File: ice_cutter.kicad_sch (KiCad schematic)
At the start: 92 parts, among them J1 Conn_01x01_Male, J2 Barrel_Jack, J3 Conn_01x03_Male, J4 Conn_01x01_Male, J5 Conn_02x03_Odd_Even, M1 Motor_Servo, M2 Motor_Servo, Q1 Q_PMOS_GSD, Q10 Q_NPN_EBC, Q11 Q_NMOS_GSD, Q2 Q_PMOS_GSD, Q3 Q_PMOS_GSD, Q4 Q_PNP_EBC, Q5 Q_NMOS_GSD, Q6 Q_PNP_EBC, Q7 Q_NMOS_GSD, Q8 Q_NPN_EBC, Q9 Q_NPN_EBC, SW1 SW_Push, SW2 SW_Push, SW3 SW_Push, U1 LM317_TO-252, U10 TMP117, U11 TM1620, U2 LM317_TO-252, U3 INA219AxD, U4 LM317_TO-252, U5 INA219AxD, U6 FJ4301AH, U7 FJ4301AH, U8 STM32G030XX, U9 SHT30-DIS

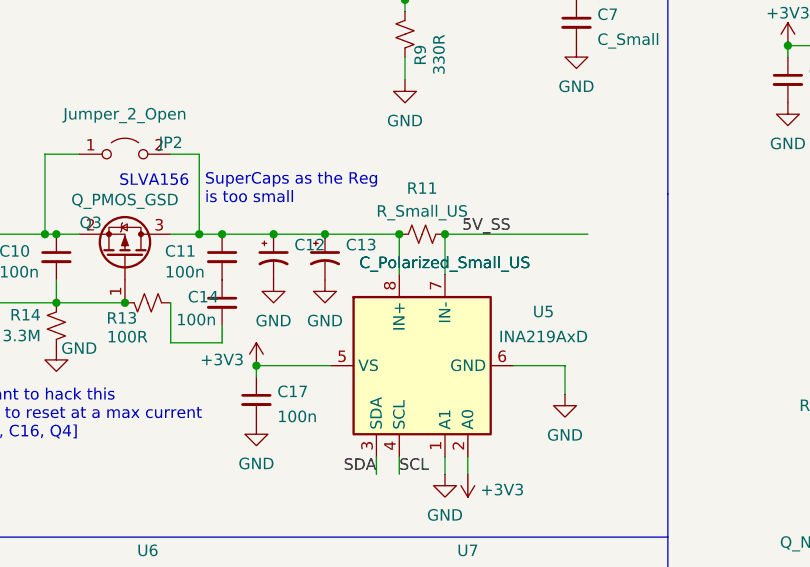
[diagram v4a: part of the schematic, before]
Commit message: added barrel jack and super caps
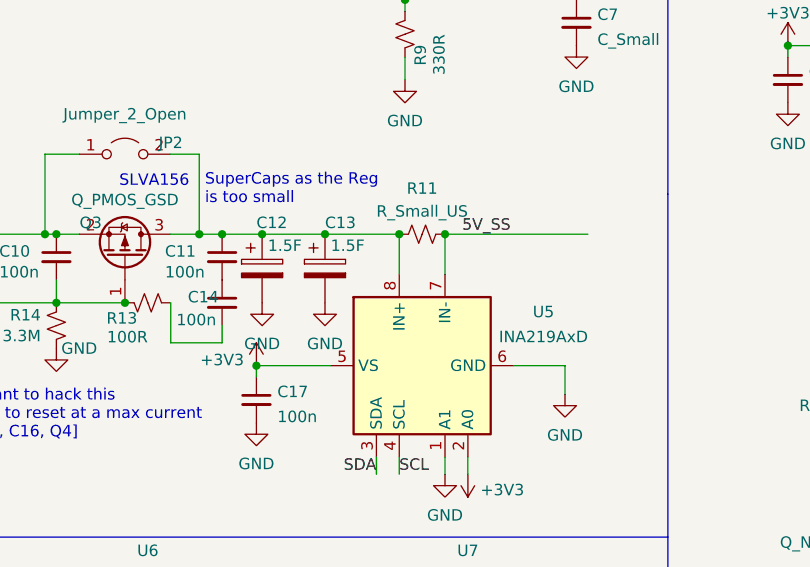
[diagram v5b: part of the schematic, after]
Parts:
- removed C12, C13: C_Polarized_Small_US, symbol Device:C_Polarized_Small_US
- added C12, C13: 1.5F, MyLibs:SP-5R5-Z155VY, symbol Device:C_Polarized
- J2: footprint (none) -> UCT:Barrel_Jack_2A_C84007
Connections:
- net GND: now also C12.2, C13.2
- net at C11.1, JP2.2 (B), Q3.3 (D)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: now also C12.1, C13.1
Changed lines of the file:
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@@
   (junction (at 238.76 148.59) (diameter 0) (color 0 0 0 0)
   )
+  (junction (at 161.29 60.325) (diameter 0) (color 0 0 0 0)
+  )
   (junction (at 181.61 60.325) (diameter 0) (color 0 0 0 0)
   )
   (junction (at 247.65 143.51) (diameter 0) (color 0 0 0 0)
   )
-  (junction (at 162.56 60.325) (diameter 0) (color 0 0 0 0)
-  )
   (junction (at 261.62 143.51) (diameter 0) (color 0 0 0 0)
   )
@@
   (junction (at 125.73 60.325) (diameter 0) (color 0 0 0 0)
   )
+  (junction (at 168.275 60.325) (diameter 0) (color 0 0 0 0)
+  )
   (junction (at 248.92 92.71) (diameter 0) (color 0 0 0 0)
   )
@@
   (junction (at 120.65 60.325) (diameter 0) (color 0 0 0 0)
   )
-  (junction (at 168.275 60.325) (diameter 0) (color 0 0 0 0)
-  )
   (junction (at 138.43 60.325) (diameter 0) (color 0 0 0 0)
   )
@@
     (stroke (width 0) (type default) (color 0 0 0 0))
   )
-  (wire (pts (xy 156.845 60.325) (xy 162.56 60.325))
-    (stroke (width 0) (type default) (color 0 0 0 0))
-  )
   (wire (pts (xy 27.305 75.565) (xy 33.655 75.565))
     (stroke (width 0) (type default) (color 0 0 0 0))
@@
     (stroke (width 0) (type default) (color 0 0 0 0))
   )
-  (wire (pts (xy 168.275 60.325) (xy 176.53 60.325))
+  (wire (pts (xy 156.845 60.325) (xy 161.29 60.325))
     (stroke (width 0) (type default) (color 0 0 0 0))
   )
@@
     (stroke (width 0) (type default) (color 0 0 0 0))
   )
+  (wire (pts (xy 168.275 60.325) (xy 176.53 60.325))
+    (stroke (width 0) (type default) (color 0 0 0 0))
+  )
   (wire (pts (xy 46.355 34.925) (xy 38.735 34.925))
     (stroke (width 0) (type default) (color 0 0 0 0))
@@
     (stroke (width 0) (type default) (color 0 0 0 0))
   )
-  (wire (pts (xy 162.56 60.325) (xy 168.275 60.325))
-    (stroke (width 0) (type default) (color 0 0 0 0))
-  )
   (polyline (pts (xy 87.63 55.88) (xy 87.63 87.63))
     (stroke (width 0) (type default) (color 0 0 0 0))
@@
     (stroke (width 0) (type default) (color 0 0 0 0))
   )
+  (wire (pts (xy 161.29 60.325) (xy 168.275 60.325))
+    (stroke (width 0) (type default) (color 0 0 0 0))
+  )
   (wire (pts (xy 81.915 169.545) (xy 81.915 172.72))
     (stroke (width 0) (type default) (color 0 0 0 0))
@@
     (pin "1")
   )
+  (symbol (lib_id "Device:C_Polarized") (at 168.275 64.135 0) (unit 1)
+    (in_bom yes) (on_board yes)
+    (property "Reference" "C13" (id 0) (at 168.275 59.055 0)
+      (effects (font (size 1.27 1.27)) (justify left))
+    )
+    (property "Value" "1.5F" (id 1) (at 168.91 61.595 0)
+      (effects (font (size 1.27 1.27)) (justify left))
+    )
+    (property "Footprint" "MyLibs:SP-5R5-Z155VY" (id 2) (at 169.2402 67.945 0)
+      (effects (font (size 1.27 1.27)) hide)
+    )
+    (property "Datasheet" "~" (id 3) (at 168.275 64.135 0)
+      (effects (font (size 1.27 1.27)) hide)
+    )
+    (property "LCSC" "C128277" (id 4) (at 168.275 64.135 0)
+      (effects (font (size 1.27 1.27)) hide)
+    )
+    (property "Populate" "Yes" (id 5) (at 168.275 64.135 0)
+      (effects (font (size 1.27 1.27)) hide)
+    )
+    (property "Price" "1.35" (id 6) (at 168.275 64.135 0)
+      (effects (font (size 1.27 1.27)) hide)
+    )
+    (pin "1")
+    (pin "2")
+  )
   (symbol (lib_id "Device:C_Small") (at 219.71 43.18 0) (unit 1)
     (in_bom yes) (on_board yes) (fields_autoplaced)
@@
     (pin "8")
   )
-  (symbol (lib_id "Device:C_Polarized_Small_US") (at 168.275 62.865 0) (unit 1)
-    (in_bom yes) (on_board yes)
-    (property "Reference" "C13" (id 0) (at 170.5864 61.5247 0)
-      (effects (font (size 1.27 1.27)) (justify left))
-    )
-    (property "Value" "C_Polarized_Small_US" (id 1) (at 172.085 63.5 0)
-      (effects (font (size 1.27 1.27)) (justify left))
-    )
-    (property "Footprint" "" (id 2) (at 168.275 62.865 0)
-      (effects (font (size 1.27 1.27)) hide)
-    )
-    (property "Datasheet" "~" (id 3) (at 168.275 62.865 0)
-      (effects (font (size 1.27 1.27)) hide)
-    )
-    (property "Populate" "Yes" (id 4) (at 168.275 62.865 0)
-      (effects (font (size 1.27 1.27)) hide)
-    )
-    (pin "1")
-    (pin "2")
-  )
   (symbol (lib_id "power:+5V") (at 91.44 71.755 0) (unit 1)
     (in_bom yes) (on_board yes)
@@
     (pin "2")
   )
+  (symbol (lib_id "Device:C_Polarized") (at 161.29 64.135 0) (unit 1)
+    (in_bom yes) (on_board yes)
+    (property "Reference" "C12" (id 0) (at 160.655 59.055 0)
+      (effects (font (size 1.27 1.27)) (justify left))
+    )
+    (property "Value" "1.5F" (id 1) (at 161.925 61.595 0)
+      (effects (font (size 1.27 1.27)) (justify left))
+    )
+    (property "Footprint" "MyLibs:SP-5R5-Z155VY" (id 2) (at 162.2552 67.945 0)
+      (effects (font (size 1.27 1.27)) hide)
+    )
+    (property "Datasheet" "~" (id 3) (at 161.29 64.135 0)
+      (effects (font (size 1.27 1.27)) hide)
+    )
+    (property "LCSC" "C128277" (id 4) (at 161.29 64.135 0)
+      (effects (font (size 1.27 1.27)) hide)
+    )
+    (property "Populate" "Yes" (id 5) (at 161.29 64.135 0)
+      (effects (font (size 1.27 1.27)) hide)
+    )
+    (property "Price" "1.35" (id 6) (at 161.29 64.135 0)
+      (effects (font (size 1.27 1.27)) hide)
+    )
+    (pin "1")
+    (pin "2")
+  )
   (symbol (lib_id "Device:C_Small") (at 57.15 34.925 0) (unit 1)
     (in_bom yes) (on_board yes)
@@
     (property "Reference" "J2" (id 0) (at 19.685 22.0685 0))
     (property "Value" "Barrel_Jack" (id 1) (at 19.685 24.8436 0))
-    (property "Footprint" "" (id 2) (at 20.955 30.861 0)
+    (property "Footprint" "UCT:Barrel_Jack_2A_C84007" (id 2) (at 20.955 30.861 0)
       (effects (font (size 1.27 1.27)) hide)
     )
@@
     (pin "2")
   )
-  (symbol (lib_id "power:GND") (at 162.56 65.405 0) (unit 1)
+  (symbol (lib_id "power:GND") (at 161.29 67.945 0) (unit 1)
     (in_bom yes) (on_board yes) (fields_autoplaced)
-    (property "Reference" "#PWR028" (id 0) (at 162.56 71.755 0)
+    (property "Reference" "#PWR028" (id 0) (at 161.29 74.295 0)
       (effects (font (size 1.27 1.27)) hide)
     )
-    (property "Value" "GND" (id 1) (at 162.56 69.9675 0))
-    (property "Footprint" "" (id 2) (at 162.56 65.405 0)
+    (property "Value" "GND" (id 1) (at 161.29 72.5075 0))
+    (property "Footprint" "" (id 2) (at 161.29 67.945 0)
       (effects (font (size 1.27 1.27)) hide)
     )
-    (property "Datasheet" "" (id 3) (at 162.56 65.405 0)
+    (property "Datasheet" "" (id 3) (at 161.29 67.945 0)
       (effects (font (size 1.27 1.27)) hide)
     )
@@
     (pin "1")
   )
-  (symbol (lib_id "Device:C_Polarized_Small_US") (at 162.56 62.865 0) (unit 1)
-    (in_bom yes) (on_board yes)
-    (property "Reference" "C12" (id 0) (at 164.8714 61.5247 0)
-      (effects (font (size 1.27 1.27)) (justify left))
-    )
-    (property "Value" "C_Polarized_Small_US" (id 1) (at 172.085 63.5 0)
-      (effects (font (size 1.27 1.27)) (justify left))
-    )
-    (property "Footprint" "" (id 2) (at 162.56 62.865 0)
-      (effects (font (size 1.27 1.27)) hide)
-    )
-    (property "Datasheet" "~" (id 3) (at 162.56 62.865 0)
-      (effects (font (size 1.27 1.27)) hide)
-    )
-    (property "Populate" "Yes" (id 4) (at 162.56 62.865 0)
-      (effects (font (size 1.27 1.27)) hide)
-    )
-    (pin "1")
-    (pin "2")
-  )
   (symbol (lib_id "power:+3V3") (at 219.71 39.37 0) (unit 1)
     (in_bom yes) (on_board yes) (fields_autoplaced)
@@
     (pin "1")
   )
-  (symbol (lib_id "power:GND") (at 168.275 65.405 0) (unit 1)
+  (symbol (lib_id "power:GND") (at 168.275 67.945 0) (unit 1)
     (in_bom yes) (on_board yes) (fields_autoplaced)
-    (property "Reference" "#PWR029" (id 0) (at 168.275 71.755 0)
+    (property "Reference" "#PWR029" (id 0) (at 168.275 74.295 0)
       (effects (font (size 1.27 1.27)) hide)
     )
-    (property "Value" "GND" (id 1) (at 168.275 69.9675 0))
-    (property "Footprint" "" (id 2) (at 168.275 65.405 0)
+    (property "Value" "GND" (id 1) (at 168.275 72.5075 0))
+    (property "Footprint" "" (id 2) (at 168.275 67.945 0)
       (effects (font (size 1.27 1.27)) hide)
     )
-    (property "Datasheet" "" (id 3) (at 168.275 65.405 0)
+    (property "Datasheet" "" (id 3) (at 168.275 67.945 0)
       (effects (font (size 1.27 1.27)) hide)
     )
@@
       (reference "C11") (unit 1) (value "100n") (footprint "Capacitor_SMD:C_0402_1005Metric")
     )
-    (path "/97a119c1-4eb1-4a38-a2a8-f2b119cbcb67"
-      (reference "C12") (unit 1) (value "C_Polarized_Small_US") (footprint "")
+    (path "/4f66cf15-7f3b-4b56-a1e8-64c6c9dcdf1a"
+      (reference "C12") (unit 1) (value "1.5F") (footprint "MyLibs:SP-5R5-Z155VY")
     )
-    (path "/1bc60681-0b0e-4c89-a308-b07913afb1f1"
-      (reference "C13") (unit 1) (value "C_Polarized_Small_US") (footprint "")
+    (path "/18d8abaa-19c1-45ff-b0a6-4a9fbd8b1327"
+      (reference "C13") (unit 1) (value "1.5F") (footprint "MyLibs:SP-5R5-Z155VY")
     )
     (path "/f9ffa617-6741-41ed-aaff-361c870d69a5"
@@
     )
     (path "/74a10180-c3f0-41cf-a4cf-6307885df43d"
-      (reference "J2") (unit 1) (value "Barrel_Jack") (footprint "")
+      (reference "J2") (unit 1) (value "Barrel_Jack") (footprint "UCT:Barrel_Jack_2A_C84007")
     )
     (path "/5ece99e6-b51b-40a1-bf7e-dbdebdd0a46f"
